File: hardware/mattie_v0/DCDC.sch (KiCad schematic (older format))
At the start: 15 parts, among them J1 5V, J3 Power, SW2 USB_POWER, U3 MCP1826T, U4 MCP1826S-3302

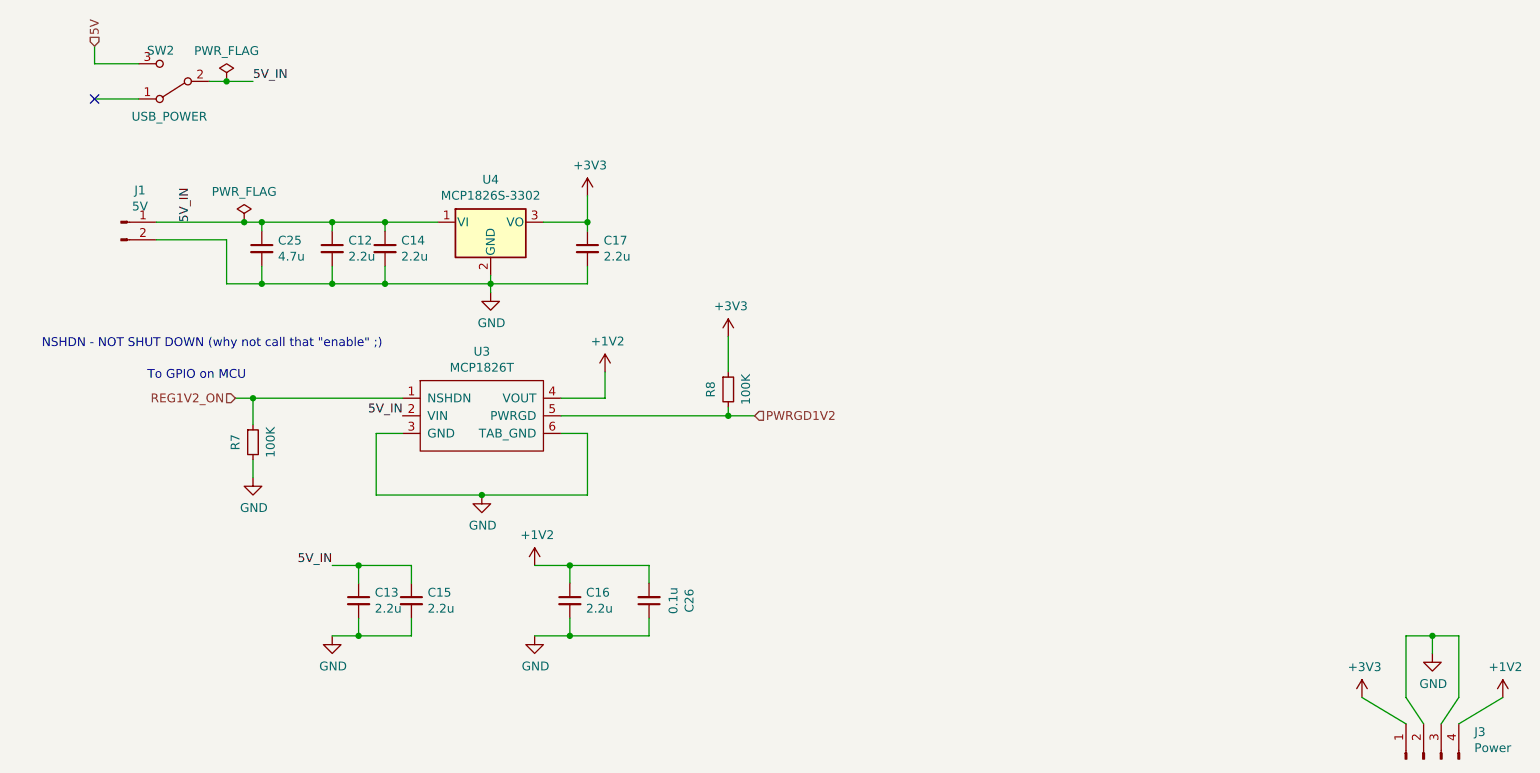
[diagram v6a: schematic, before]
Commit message: Changed some cap values and added extra caps
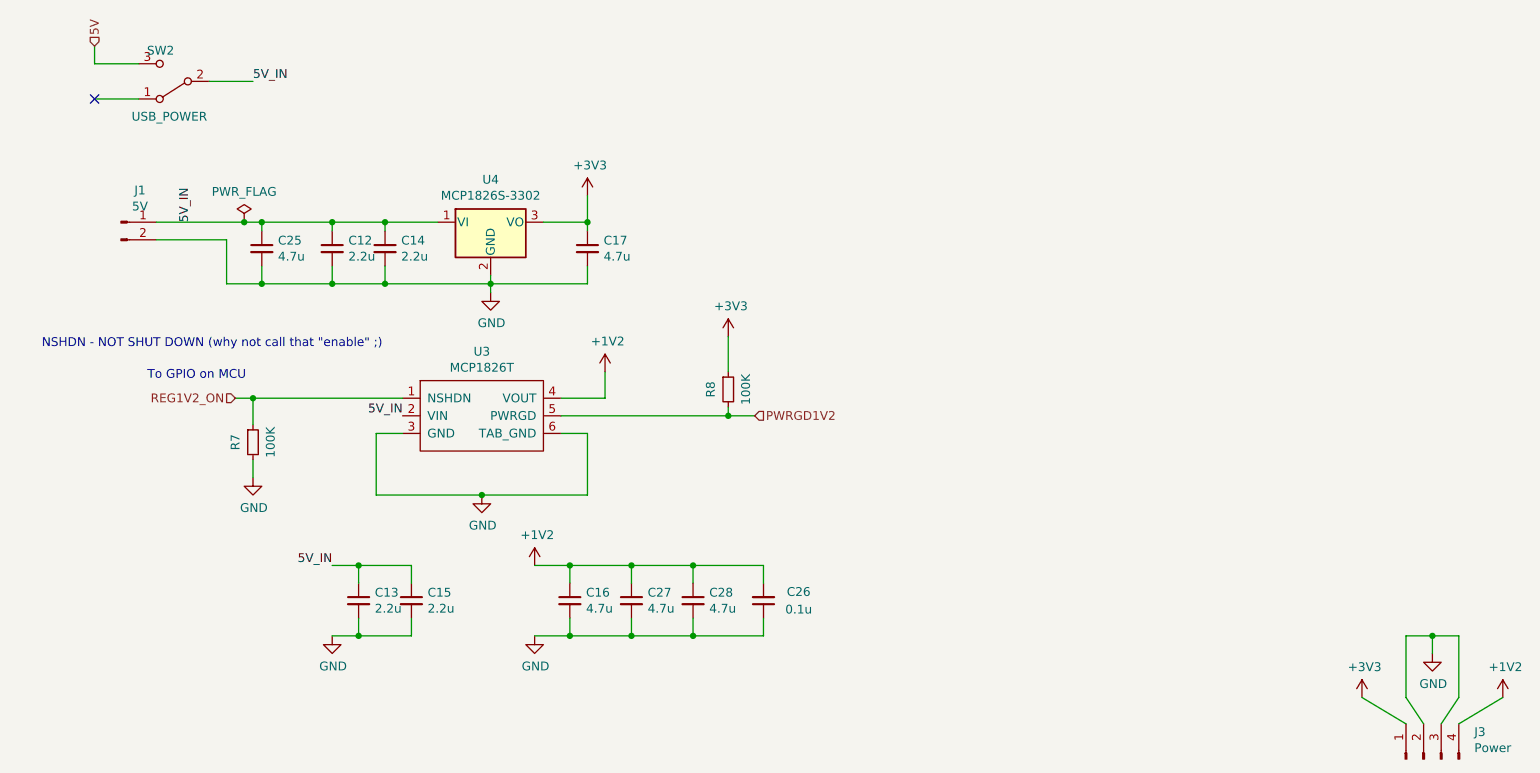
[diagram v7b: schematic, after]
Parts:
- added C27, C28: 4.7u, Capacitor_SMD:C_0603_1608Metric, symbol Device:C_Small
- C16, C17: value 2.2u -> 4.7u; OrderN 963-TMK107ABJ225MA-T -> 346-CM105X5R475M25AT
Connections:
- net +1V2: now also C27.1, C28.1
- net GND: now also C27.2, C28.2
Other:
- moved on the sheet: C26
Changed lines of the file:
@@
-	1    0    0    -1
-$EndComp
-$Comp
-L Device:C_Small C?
-U 1 1 5E9F0723
-P 4250 2850
-AR Path="/5E994520/5E9F0723" Ref="C?"  Part="1"
-AR Path="/5E9881B4/5E9F0723" Ref="C?"  Part="1"
-AR Path="/5E988213/5E9F0723" Ref="C17"  Part="1"
-F 0 "C17" H 4342 2896 50  0000 L CNN
-F 1 "2.2u" H 4342 2805 50  0000 L CNN
-F 2 "Capacitor_SMD:C_0603_1608Metric" H 4250 2850 50  0001 C CNN
-F 3 "~" H 4250 2850 50  0001 C CNN
-F 4 " 963-TMK107ABJ225MA-T " H 4250 2850 50  0001 C CNN "OrderN"
-	1    4250 2850
 	1    0    0    -1
 $EndComp
@@
 $Comp
 L Device:C_Small C?
-U 1 1 5E9CDDC4
-P 4150 4850
-AR Path="/5E994520/5E9CDDC4" Ref="C?"  Part="1"
-AR Path="/5E9881B4/5E9CDDC4" Ref="C?"  Part="1"
-AR Path="/5E988213/5E9CDDC4" Ref="C16"  Part="1"
-F 0 "C16" H 4242 4896 50  0000 L CNN
-F 1 "2.2u" H 4242 4805 50  0000 L CNN
-F 2 "Capacitor_SMD:C_0603_1608Metric" H 4150 4850 50  0001 C CNN
-F 3 "~" H 4150 4850 50  0001 C CNN
-F 4 " 963-TMK107ABJ225MA-T " H 4150 4850 50  0001 C CNN "OrderN"
-	1    4150 4850
-	1    0    0    -1
-$EndComp
-$Comp
-L Device:C_Small C?
 U 1 1 5E9CE26F
 P 3250 4850
@@
 	2200 2800 2200 3050
 Connection ~ 2400 3050
-Wire Wire Line
-	2100 1900 2200 1900
-$Comp
-L power:PWR_FLAG #FLG0101
-U 1 1 5EA83F67
-P 2200 1900
-F 0 "#FLG0101" H 2200 1975 50  0001 C CNN
-F 1 "PWR_FLAG" H 2200 2073 50  0000 C CNN
-F 2 "" H 2200 1900 50  0001 C CNN
-F 3 "~" H 2200 1900 50  0001 C CNN
-	1    2200 1900
-	1    0    0    -1
-$EndComp
-Connection ~ 2200 1900
-Wire Wire Line
-	2200 1900 2350 1900
 $Comp
 L power:PWR_FLAG #FLG0104
@@
 L Device:C_Small C?
 U 1 1 5EA1D6AA
-P 4600 4850
+P 5250 4850
 AR Path="/5E9881B4/5EA1D6AA" Ref="C?"  Part="1"
 AR Path="/5E98823A/5EA1D6AA" Ref="C?"  Part="1"
 AR Path="/5E988213/5EA1D6AA" Ref="C26"  Part="1"
-F 0 "C26" V 4371 4850 50  0000 C CNN
-F 1 "0.1u" V 4462 4850 50  0000 C CNN
-F 2 "Capacitor_SMD:C_0603_1608Metric" H 4600 4850 50  0001 C CNN
-F 3 "~" H 4600 4850 50  0001 C CNN
-F 4 " 963-TMK107BJ104KA-T " H 4600 4850 50  0001 C CNN "Mouser"
-	1    4600 4850
+F 0 "C26" H 5050 4800 50  0000 C CNN
+F 1 "0.1u" H 5050 4900 50  0000 C CNN
+F 2 "Capacitor_SMD:C_0603_1608Metric" H 5250 4850 50  0001 C CNN
+F 3 "~" H 5250 4850 50  0001 C CNN
+F 4 " 963-TMK107BJ104KA-T " H 5250 4850 50  0001 C CNN "Mouser"
+	1    5250 4850
 	-1   0    0    1
 $EndComp
 Wire Wire Line
-	4600 4750 4600 4650
-Wire Wire Line
-	4600 4650 4150 4650
-Connection ~ 4150 4650
-Wire Wire Line
-	4600 4950 4600 5050
-Wire Wire Line
-	4600 5050 4150 5050
-Connection ~ 4150 5050
+	5250 4750 5250 4650
+Wire Wire Line
+	5250 4950 5250 5050
 Text Label 2000 2700 1    50   ~ 0
 5V_IN
+$Comp
+L Device:C_Small C?
+U 1 1 5EA248DA
+P 4250 2850
+AR Path="/5E994520/5EA248DA" Ref="C?"  Part="1"
+AR Path="/5E9881B4/5EA248DA" Ref="C?"  Part="1"
+AR Path="/5E988213/5EA248DA" Ref="C17"  Part="1"
+F 0 "C17" H 4342 2896 50  0000 L CNN
+F 1 "4.7u" H 4342 2805 50  0000 L CNN
+F 2 "Capacitor_SMD:C_0603_1608Metric" H 4250 2850 50  0001 C CNN
+F 3 "~" H 4250 2850 50  0001 C CNN
+F 4 " 346-CM105X5R475M25AT " H 4250 2850 50  0001 C CNN "OrderN"
+	1    4250 2850
+	1    0    0    -1
+$EndComp
+$Comp
+L Device:C_Small C?
+U 1 1 5EA24FB5
+P 4150 4850
+AR Path="/5E994520/5EA24FB5" Ref="C?"  Part="1"
+AR Path="/5E9881B4/5EA24FB5" Ref="C?"  Part="1"
+AR Path="/5E988213/5EA24FB5" Ref="C16"  Part="1"
+F 0 "C16" H 4242 4896 50  0000 L CNN
+F 1 "4.7u" H 4242 4805 50  0000 L CNN
+F 2 "Capacitor_SMD:C_0603_1608Metric" H 4150 4850 50  0001 C CNN
+F 3 "~" H 4150 4850 50  0001 C CNN
+F 4 " 346-CM105X5R475M25AT " H 4150 4850 50  0001 C CNN "OrderN"
+	1    4150 4850
+	1    0    0    -1
+$EndComp
+$Comp
+L Device:C_Small C?
+U 1 1 5EA2F64D
+P 4500 4850
+AR Path="/5E994520/5EA2F64D" Ref="C?"  Part="1"
+AR Path="/5E9881B4/5EA2F64D" Ref="C?"  Part="1"
+AR Path="/5E988213/5EA2F64D" Ref="C27"  Part="1"
+F 0 "C27" H 4592 4896 50  0000 L CNN
+F 1 "4.7u" H 4592 4805 50  0000 L CNN
+F 2 "Capacitor_SMD:C_0603_1608Metric" H 4500 4850 50  0001 C CNN
+F 3 "~" H 4500 4850 50  0001 C CNN
+F 4 " 346-CM105X5R475M25AT " H 4500 4850 50  0001 C CNN "OrderN"
+	1    4500 4850
+	1    0    0    -1
+$EndComp
+$Comp
+L Device:C_Small C?
+U 1 1 5EA2FABC
+P 4850 4850
+AR Path="/5E994520/5EA2FABC" Ref="C?"  Part="1"
+AR Path="/5E9881B4/5EA2FABC" Ref="C?"  Part="1"
+AR Path="/5E988213/5EA2FABC" Ref="C28"  Part="1"
+F 0 "C28" H 4942 4896 50  0000 L CNN
+F 1 "4.7u" H 4942 4805 50  0000 L CNN
+F 2 "Capacitor_SMD:C_0603_1608Metric" H 4850 4850 50  0001 C CNN
+F 3 "~" H 4850 4850 50  0001 C CNN
+F 4 " 346-CM105X5R475M25AT " H 4850 4850 50  0001 C CNN "OrderN"
+	1    4850 4850
+	1    0    0    -1
+$EndComp
+Wire Wire Line
+	4150 4650 4500 4650
+Connection ~ 4150 4650
+Wire Wire Line
+	4150 5050 4500 5050
+Connection ~ 4150 5050
+Wire Wire Line
+	4500 5050 4500 4950
+Wire Wire Line
+	4500 4750 4500 4650
+Wire Wire Line
+	4850 4750 4850 4650
+Wire Wire Line
+	4850 4950 4850 5050
+Wire Wire Line
+	4850 4650 5250 4650
+Wire Wire Line
+	4850 5050 5250 5050
+Wire Wire Line
+	4850 4650 4500 4650
+Connection ~ 4850 4650
+Connection ~ 4500 4650
+Wire Wire Line
+	4850 5050 4500 5050
+Connection ~ 4850 5050
+Connection ~ 4500 5050
+Wire Wire Line
+	2100 1900 2350 1900
 $EndSCHEMATC

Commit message: tweaks
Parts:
- C26: Mouser 963-TMK107BJ104KA-T -> (none); OrderN (none) -> 963-TMK107BJ104KA-T
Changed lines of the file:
@@
 F 2 "Capacitor_SMD:C_0603_1608Metric" H 5250 4850 50  0001 C CNN
 F 3 "~" H 5250 4850 50  0001 C CNN
-F 4 " 963-TMK107BJ104KA-T " H 5250 4850 50  0001 C CNN "Mouser"
+F 4 "" H 5250 4850 50  0001 C CNN "Mouser"
+F 5 " 963-TMK107BJ104KA-T " H 5250 4850 50  0001 C CNN "OrderN"
 	1    5250 4850
 	-1   0    0    1
